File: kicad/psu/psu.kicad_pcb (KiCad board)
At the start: 2 copper layers, 90 x 50 mm, 34 parts, among them J1 AC IN 12-15V, J2 DC IN 12V, J3 DC OUT 1, J4 DC OUT 2, J5 LED REMOTE, Q1 BC547, Q2 TIP41C, Q3 BC547

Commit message: Rotate screw terminals to face the board edge, add 3D views, schematics and layouts to the README, CircuitJS links in the review
Amp board is 100 x 85 mm after the hybrid-footprint courtyards grew; input header moved to open space
on the bottom edge so freerouting completes. Panel 134 x 137 mm, DRC clean.
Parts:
- moved J2 5.00 mm to (133.5, 63.0), turned to 90 degrees
- moved J3 5.00 mm to (133.5, 77.0), turned to 90 degrees
- moved J4 5.00 mm to (133.5, 91.0), turned to 90 degrees
- moved C1 2.00 mm to (102.3, 64.8)
- moved C2 2.00 mm to (116.7, 64.8)
- moved D1 1.00 mm to (64.2, 62.9)
- moved D2 1.00 mm to (81.9, 62.9)
- moved D3 1.00 mm to (64.2, 69.6)
- moved D4 1.00 mm to (81.9, 69.6)
- moved J1 0.50 mm to (56.0, 64.0), turned to -90 degrees
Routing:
- net Net-(D1-K): track 142.8 -> 152.8 mm
- net /AC2: track 53.3 -> 47.1 mm
- net Net-(Q2-E): track 73.8 -> 68.3 mm
- net Net-(D8-A): track 27.0 -> 22.0 mm
- net Net-(Q1-E): track 56.4 -> 52.8 mm, vias 1 -> 0
- net Net-(D6-A): track 104.9 -> 103.0 mm
- net GND: track 174.8 -> 175.8 mm

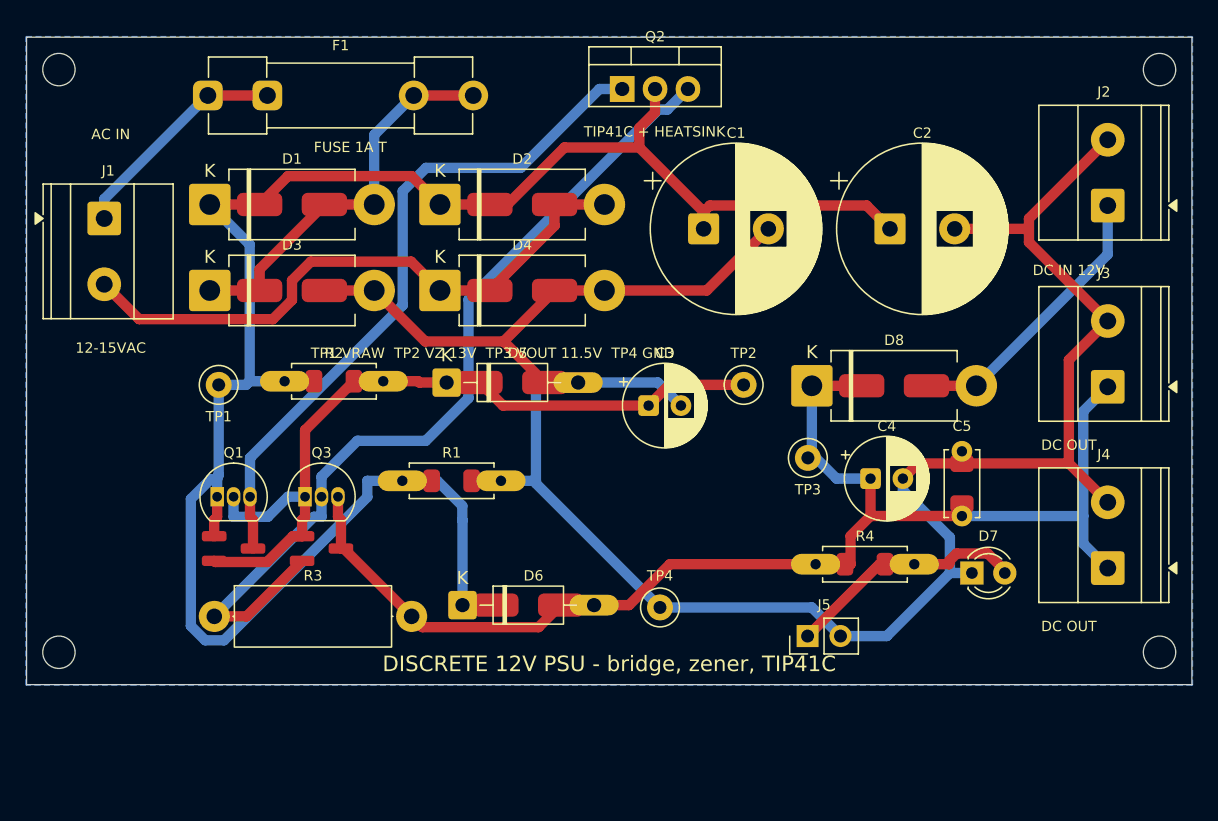
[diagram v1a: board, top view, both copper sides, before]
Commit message: Square 144 x 144 mm panel with rails; amp widened to 134 x 71 mm so PSU plus volume board match its width; readable silkscreen
References sit inside resistor, diode and ceramic outlines along the body axis, larger text; electrolytic,
transistor and test-point labels stay beside the part. Hybrid footprints built from the library parts keep
polarity marks. All 2-layer boards, the panel and the single-sided PSU and volume boards are DRC clean.
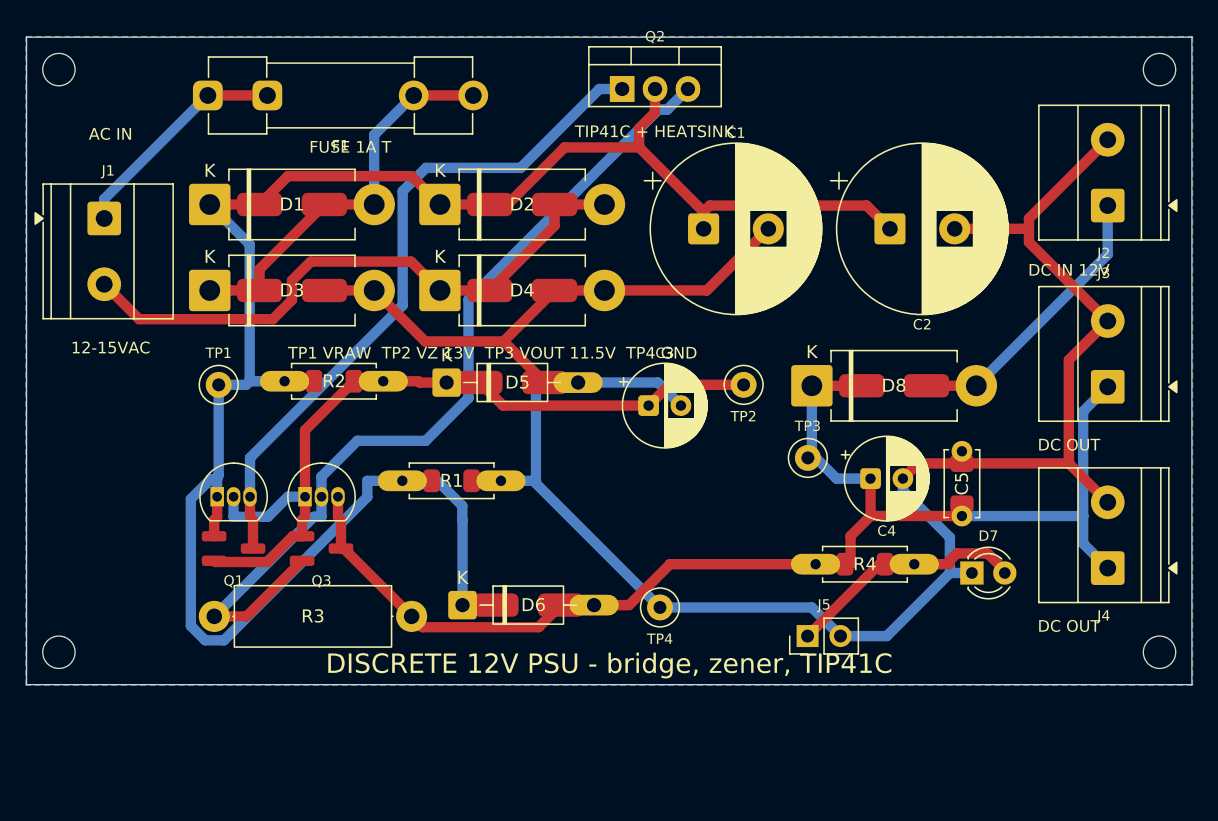
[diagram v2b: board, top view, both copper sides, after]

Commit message: Repository URL and revision on every silkscreen and on the panel rails
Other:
- board text added: "discrete-stereo-amp v1.0 2026-10"
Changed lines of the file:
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@@
 		(layer "Edge.Cuts")
+	)
+	(gr_text "discrete-stereo-amp v1.0 2026-10"
+		(at 112.95 51.95 0)
+		(layer "F.SilkS")
+		(effects
+			(font
+				(size 0.8 0.8)
+				(thickness 0.12)
+			)
+		)
 	)
 	(gr_text "AC IN"

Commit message: Release 1.1: square panel, rotated terminals, readable silkscreen, URL and revision stamps
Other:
- board text added: "discrete-stereo-amp v1.1 2026-10"
- board text removed: "discrete-stereo-amp v1.0 2026-10"
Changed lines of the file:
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@@
 		(layer "Edge.Cuts")
 	)
-	(gr_text "discrete-stereo-amp v1.0 2026-10"
+	(gr_text "discrete-stereo-amp v1.1 2026-10"
 		(at 112.95 51.95 0)
 		(layer "F.SilkS")

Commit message: Release 1.2: mirror-loaded front end, closed-loop PSU, VU tap, headphone board
- Amp: PNP input pair with NPN current-mirror load, LED-referenced current-source tail,
  NPN VAS with bootstrapped load from +12V, 220p Miller + 47p lead cap (THD 0.004% at 26 mW/8R,
  0.019% at 0.29 W; was 0.03 / 0.2). 1k VU meter tap per channel to header J5.
- PSU: BC547 error amplifier, 5.6 V zener fed from VOUT, 8.2k + 2k trimmer / 10k divider,
  2.2k drive, 47n/100n compensation. 12.0 V set point, 0.14 V dip on a 1 A step.
- New headphone board (DPDT switch, 120R series, DIRECT jumpers, 3.5 mm jack, panel-jack header).
- Boards: amp 134x85 / compact 100x98, PSU 90x58, hp 42x30; panel 155x155 with four boards.
  All 2-layer boards and the panel DRC clean; single-sided amp down to 15 errors.
- Toolchain: STAMP constant, reroute.sh second routing pass, rotated titles, link holes on
  jumper pads, 2 mm routing corridor per channel.
- Docs, BOMs, order guide, changelog, known issues rewritten for release 2.
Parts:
- added C6: 47n, Custom:C_P5_1206, F.Cu at (97.3, 96.7)
- added C7: 100n, Custom:C_P5_1206, F.Cu at (101.3, 96.7)
- added Q4: BC547, Custom:TO92_SOT23, F.Cu at (90.7, 93.2)
- added R5: 8.2k, Custom:R_Axial_1206, F.Cu at (65.4, 101.5)
- added R6: 10k, Custom:R_Axial_1206, F.Cu at (89.7, 101.5)
- added R7: 2.2k, Custom:R_Axial_1206, F.Cu at (65.4, 76.6)
- added RV1: 2k, Potentiometer_THT:Potentiometer_Bourns_3296W_Vertical, F.Cu at (83.9, 102.6)
- added TP5: FB 6.3V, TestPoint:TestPoint_Loop_D2.50mm_Drill1.0mm, F.Cu at (102.4, 101.7)
- C3: value 100u -> 10u; footprint Capacitor_THT:CP_Radial_D6.3mm_P2.50mm -> Custom:CE_P2_1206
- D5: value 13V 1W -> 5.6V
- TP2: value VZ 13V -> VZ 5.6V
- TP3: value VOUT 11.5V -> VOUT 12.0V
- moved TP1 63.5 mm to (123.7, 100.7)
- moved R1 35.8 mm to (110.9, 100.4)
- moved D6 28.7 mm to (110.1, 105.0)
- moved TP4 28.7 mm to (125.4, 105.2)
- moved TP2 24.5 mm to (86.3, 92.2)
- moved D5 23.5 mm to (64.6, 92.0)
- moved C3 23.4 mm to (79.9, 93.2)
- moved R2 17.4 mm to (84.5, 86.1)
- moved Q1 15.4 mm to (78.0, 77.8)
- moved Q3 15.4 mm to (84.8, 77.8)
- moved H3 8.00 mm to (52.5, 105.5)
- moved H4 8.00 mm to (137.5, 105.5)
- moved R3 7.69 mm to (64.5, 87.0)
- moved J4 4.00 mm to (133.5, 95.0)
- moved J3 2.00 mm to (133.5, 79.0)
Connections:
- C3 pad 1: /VZ -> Net-(D5-K)
- D5 pad 1: /VZ -> Net-(D5-K)
- D5 pad 1S: /VZ -> Net-(D5-K)
- Q1 pad 2: /VZ -> /BQ1
- Q1 pad 2S: /VZ -> /BQ1
- Q3 pad 1: /VZ -> /BQ1
- Q3 pad 1S: /VZ -> /BQ1
- R2 pad 1: Net-(D1-K) -> Net-(D6-A)
- R2 pad 1S: Net-(D1-K) -> Net-(D6-A)
- R2 pad 2: /VZ -> Net-(D5-K)
- R2 pad 2S: /VZ -> Net-(D5-K)
- TP2 pad 1: /VZ -> Net-(D5-K)
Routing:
- net /VZ: track 60.5 -> 0.00 mm
- net /BQ1: track 0.00 -> 58.5 mm
- net Net-(D5-K): track 0.00 -> 55.1 mm
- net Net-(Q4-B): track 0.00 -> 53.1 mm
- net Net-(D6-A): track 103.0 -> 155.7 mm
- net GND: track 175.8 -> 203.5 mm
- net Net-(Q2-E): track 68.3 -> 86.2 mm
- net Net-(R5-Pad2): track 0.00 -> 13.7 mm
- net Net-(Q1-E): track 52.8 -> 41.5 mm
- net Net-(D1-K): track 152.8 -> 163.4 mm
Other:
- board size 90 x 50 mm -> 90 x 58 mm
- board text added: "DISCRETE 12V PSU"
- board text added: "TP1 VRAW TP2 VZ 5.6V TP3 VOUT 12.0V TP5 FB 6.3V TP4 GND"
- board text added: "discrete-stereo-amp v1.2 2026-10"
- board text removed: "DISCRETE 12V PSU - bridge, zener, TIP41C"
- board text removed: "TP1 VRAW TP2 VZ 13V TP3 VOUT 11.5V TP4 GND"
- board text removed: "discrete-stereo-amp v1.1 2026-10"
